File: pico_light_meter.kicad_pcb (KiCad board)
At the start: 2 copper layers, 52.5 x 27 mm, 5 parts

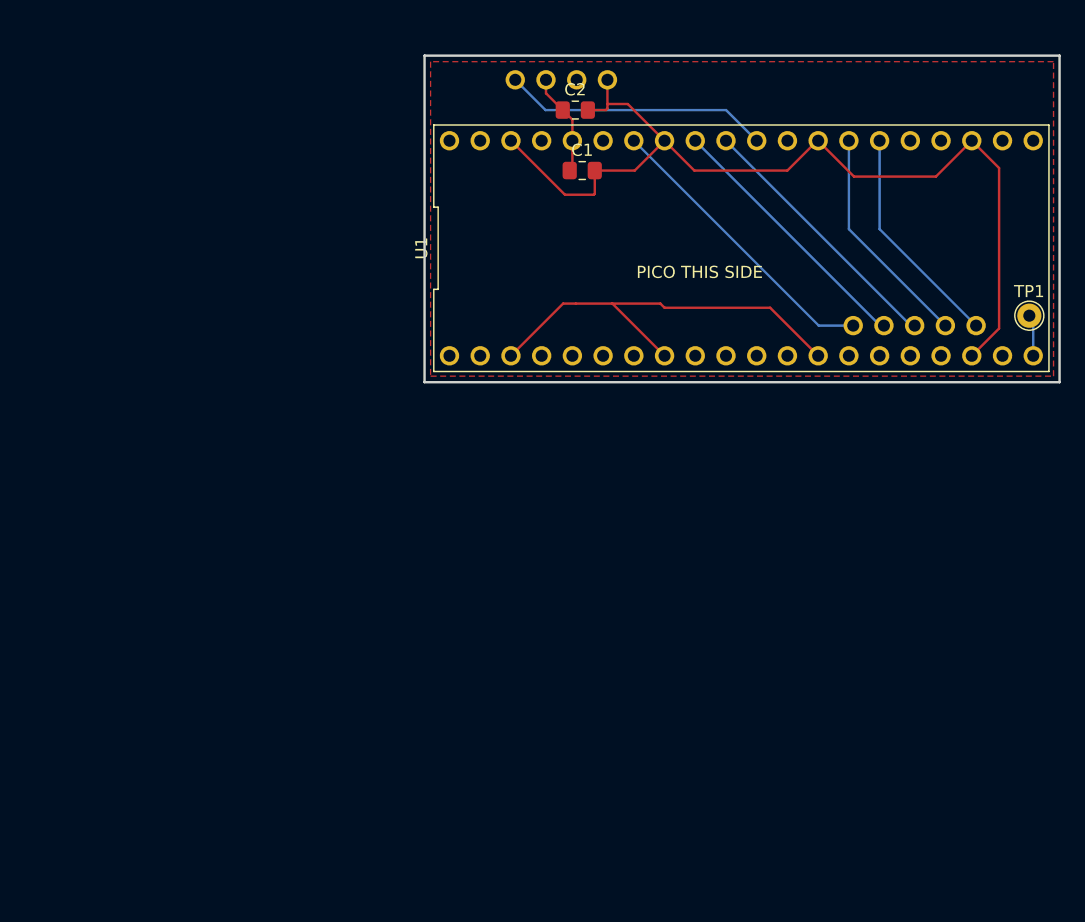
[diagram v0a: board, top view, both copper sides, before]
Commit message: Intermediate commit of routed board with Pico on top.
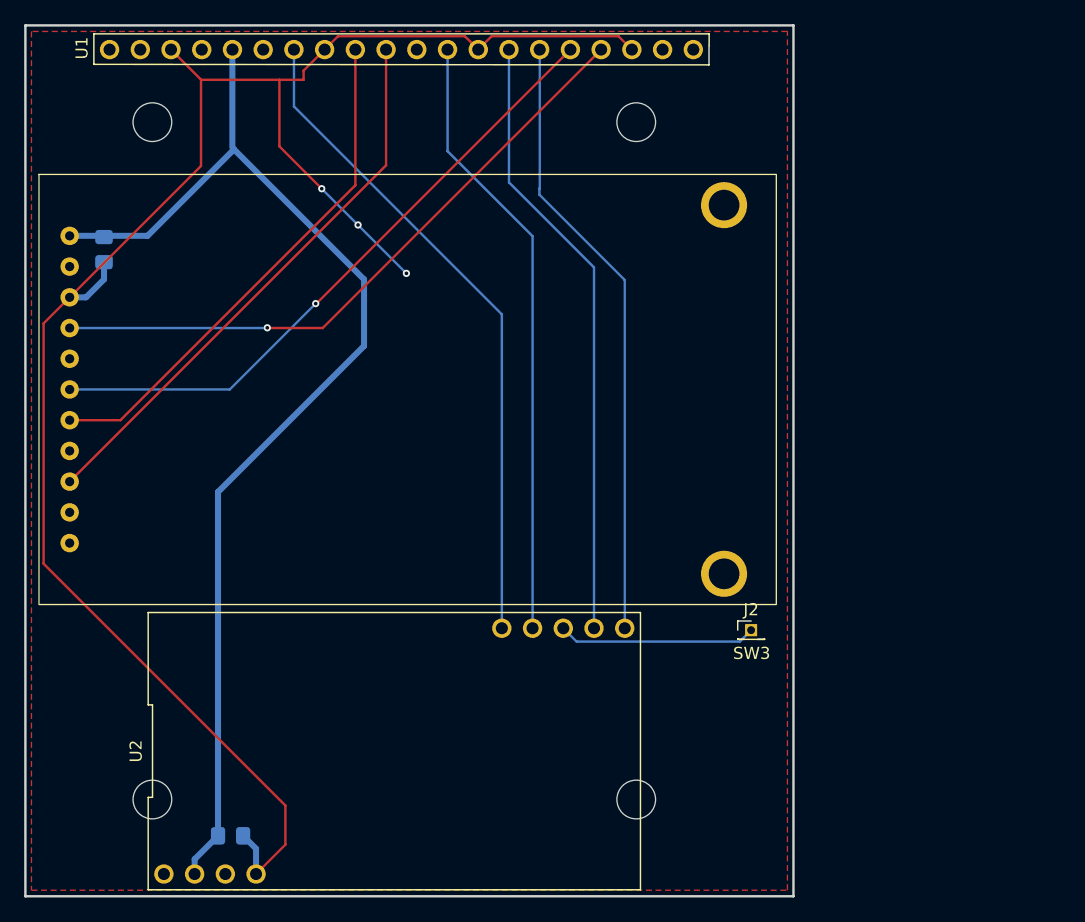
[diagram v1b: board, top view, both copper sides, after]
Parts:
- removed TP1: TestPoint, TestPoint:TestPoint_THTPad_D2.0mm_Drill1.0mm
- added H1: MountingHole, MountingHole:MountingHole_3.2mm_M3_ISO14580, F.Cu at (100.0, 50.0)
- added H2: MountingHole, MountingHole:MountingHole_3.2mm_M3_ISO14580, F.Cu at (140.0, 106.0)
- added H3: MountingHole, MountingHole:MountingHole_3.2mm_M3_ISO14580, F.Cu at (100.0, 106.0)
- added H4: MountingHole, MountingHole:MountingHole_3.2mm_M3_ISO14580, F.Cu at (140.0, 50.0)
- added J2: Conn_01x01, Connector_PinHeader_1.27mm:PinHeader_1x01_P1.27mm_Vertical, F.Cu at (149.5, 92.0)
- added U3: ~, pico_light_meter:adafruit_2.0_IPS_Display, F.Cu at (90.6, 54.3)
- C1, C2: moved to B.Cu
- U1: footprint pico_light_meter:pico2 -> pico_light_meter:pico2_right_pins_only
- U2: moved to F.Cu
- moved C2 66.4 mm to (106.5, 109.0)
- moved U2 53.8 mm to (120.0, 102.0)
- moved C1 40.1 mm to (96.0, 60.5), turned to -90 degrees
- moved U1 29.1 mm to (120.6, 52.9)
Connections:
- net /I2C0_SCL renamed /OLED_SCL
- net /I2C0_SDA renamed /OLED_SDA
- U1 pad 21: unconnected-(U1-_MISO-Pad21) -> /SD_MISO
- U1 pad 22: unconnected-(U1-_CARD_CS-Pad22) -> /SD_CS
- U1 pad 24: unconnected-(U1-_SCK-Pad24) -> /IPS_SCK
- U1 pad 25: unconnected-(U1-_MOSI-Pad25) -> /IPS_MOSI
- U1 pad 29: unconnected-(U1-_SHUTTER-Pad29) -> /COWBELL_SHUTTER
- U1 pad 31: /SW3 -> /IPS_DC
- U1 pad 32: /SW4 -> /IPS_CS
- U2 pad 1: //RESET -> unconnected-(U2-/RESET-Pad1)
- U2 pad 20: /SW4 -> /COWBELL_SHUTTER
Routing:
- net +3.3V: track 8.50 -> 95.0 mm
- net /IPS_SCK: track 0.00 -> 53.5 mm, vias 0 -> 1
- net /IPS_MOSI: track 0.00 -> 53.0 mm, vias 0 -> 1
- net /COWBELL_SHUTTER: track 0.00 -> 50.8 mm
- net /IPS_DC: track 0.00 -> 46.6 mm
- net /IPS_CS: track 0.00 -> 42.9 mm
- net GND: track 112.2 -> 151.6 mm, vias 0 -> 3
- net /OLED_SDA: track 18.6 -> 50.8 mm
- net /OLED_SCL: track 18.6 -> 50.8 mm
- net /SW2: track 24.5 -> 55.0 mm
- net //RESET: track 22.0 -> 0.00 mm
- net /SW4: track 21.9 -> 0.00 mm
- net /SW3: track 21.9 -> 16.4 mm
- net Net-(U1-GPIO15): track 3.45 -> 0.00 mm
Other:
- board size 52.5 x 27 mm -> 63.5 x 72 mm
- board text added: "SW3"
- board text removed: "OLED THIS SIDE"
- board text removed: "PICO THIS SIDE"

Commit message: Another iteration, now with Pico on bottom
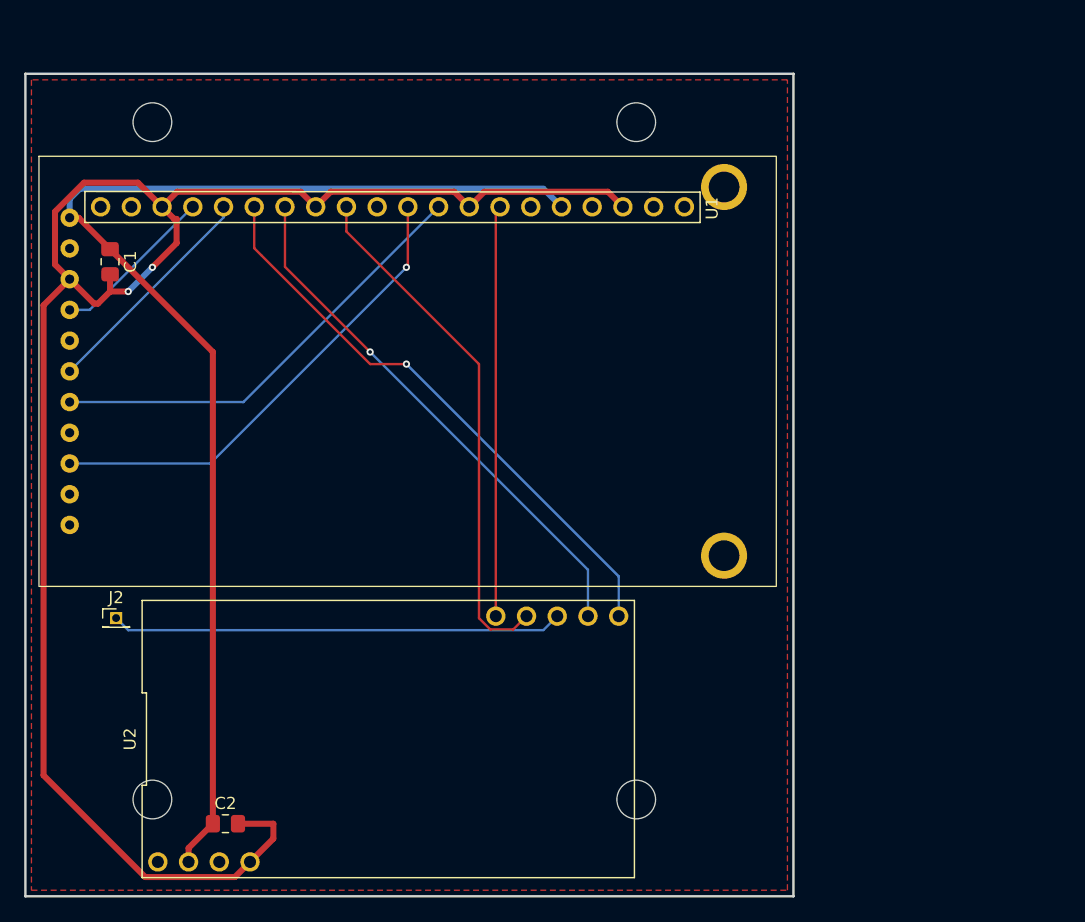
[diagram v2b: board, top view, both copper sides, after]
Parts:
- C1, C2: moved to F.Cu
- moved J2 52.5 mm to (97.0, 91.0)
- moved U1 4.84 mm to (119.8, 48.1), turned to 180 degrees
- moved U3 1.50 mm to (90.6, 52.8)
- moved C1 1.12 mm to (96.5, 61.5)
- moved U2 1.12 mm to (119.5, 101.0)
- moved C2 1.09 mm to (106.0, 108.0)
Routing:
- net /IPS_SCK: track 53.5 -> 13.7 mm, vias 1 -> 0
- net /IPS_MOSI: track 53.0 -> 18.9 mm, vias 1 -> 0
- net /SW3: track 16.4 -> 37.4 mm
- net /SW2: track 55.0 -> 34.0 mm
- net +3.3V: track 95.0 -> 102.6 mm
- net /COWBELL_SHUTTER: track 50.8 -> 43.3 mm
- net GND: track 151.6 -> 144.6 mm, vias 3 -> 2
- net /IPS_DC: track 46.6 -> 39.6 mm, vias 0 -> 1
- net /OLED_SCL: track 50.8 -> 44.2 mm, vias 0 -> 1
- net /IPS_CS: track 42.9 -> 37.2 mm
- net /OLED_SDA: track 50.8 -> 48.1 mm, vias 0 -> 1
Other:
- board size 63.5 x 72 mm -> 63.5 x 68 mm
- board text removed: "SW3"

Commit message: Updated with MCP port expander
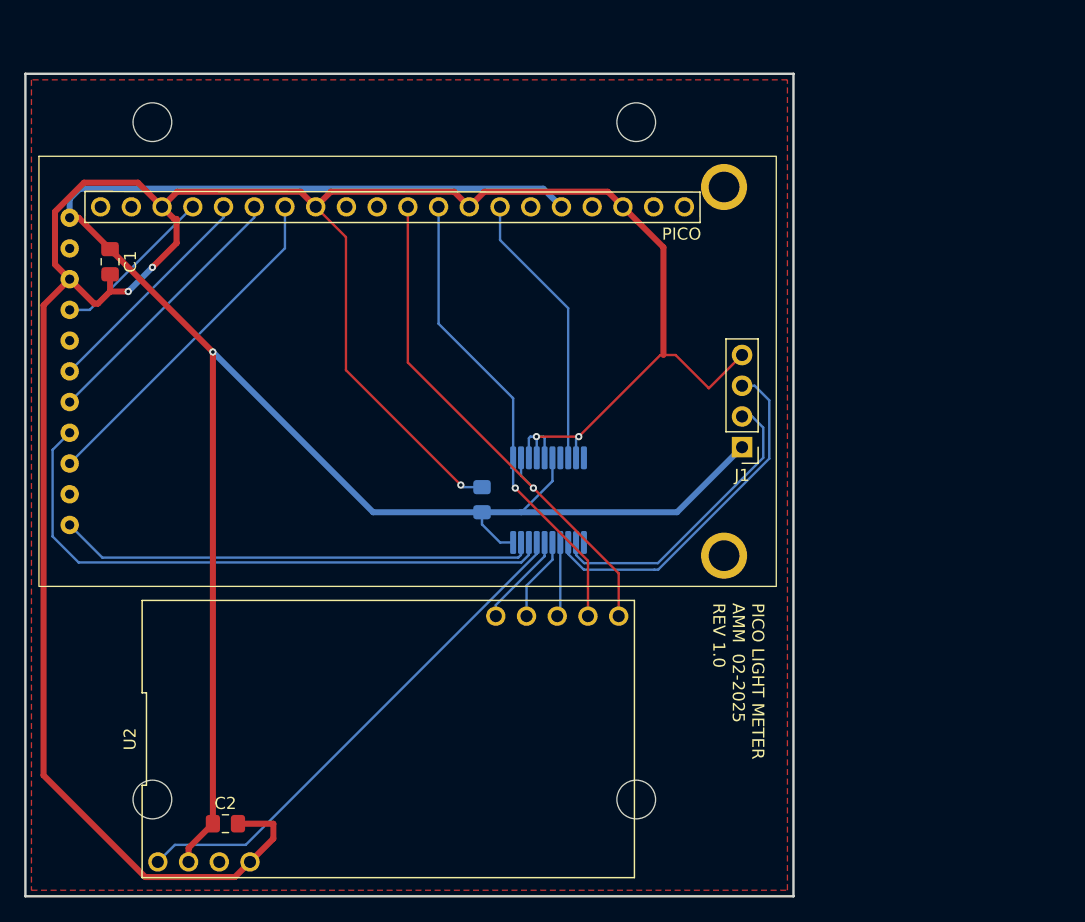
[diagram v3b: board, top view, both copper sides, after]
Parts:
- removed J2: Conn_01x01, Connector_PinHeader_1.27mm:PinHeader_1x01_P1.27mm_Vertical
- added C3: C, Capacitor_SMD:C_0805_2012Metric_Pad1.18x1.45mm_HandSolder, B.Cu at (127.2, 81.2)
- added J1: Conn_01x04, Connector_PinHeader_2.54mm:PinHeader_1x04_P2.54mm_Vertical, F.Cu at (148.8, 76.9)
- added U4: MCP23008-xSS, Package_SO:SSOP-20_5.3x7.2mm_P0.65mm, B.Cu at (132.8, 81.2)
- renumbered U1 to PICO
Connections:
- PICO pad 26: /OLED_SDA -> /IPS_CS
- PICO pad 27: /OLED_SCL -> /IPS_DC
- PICO pad 31: /IPS_DC -> /I2C1_SDA
- PICO pad 32: /IPS_CS -> /I2C1_SCL
- PICO pad 34: /SW2 -> /MCP_INT
- U2 pad 1: unconnected-(U2-/RESET-Pad1) -> /SW5
- U2 pad 17: /OLED_SDA -> /I2C1_SDA
- U2 pad 18: /OLED_SCL -> /I2C1_SCL
- U2 pad 20: /COWBELL_SHUTTER -> /SW4
- U3 pad 1: unconnected-(U3-BACKLIGHT-Pad1) -> /IPS_BACKLIGHT
- U3 pad 4: unconnected-(U3-RESET-Pad4) -> /IPS_RESET
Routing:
- net GND: track 144.6 -> 218.4 mm, vias 2 -> 5
- net +3.3V: track 102.6 -> 163.8 mm, vias 0 -> 1
- net /IPS_RESET: track 0.00 -> 50.7 mm
- net /OLED_SDA: track 48.1 -> 0.00 mm, vias 1 -> 0
- net /OLED_SCL: track 44.2 -> 0.00 mm, vias 1 -> 0
- net /I2C1_SDA: track 0.00 -> 44.0 mm, vias 0 -> 1
- net /COWBELL_SHUTTER: track 43.3 -> 0.00 mm
- net /SW5: track 0.00 -> 42.8 mm
- net /IPS_BACKLIGHT: track 0.00 -> 39.6 mm
- net /I2C1_SCL: track 0.00 -> 39.0 mm, vias 0 -> 1
- net /SW3: track 37.4 -> 6.20 mm
- net Net-(J1-Pin_3): track 0.00 -> 29.5 mm
- net /SW2: track 34.0 -> 7.92 mm
- net Net-(J1-Pin_2): track 0.00 -> 25.0 mm
- net /MCP_INT: track 0.00 -> 23.6 mm
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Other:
- board text added: "PICO LIGHT METER AMM 02-2025 REV 1.0"

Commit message: Big update to board
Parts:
- C1, C2: moved to B.Cu
- C3, U4: moved to F.Cu
- U3: footprint pico_light_meter:adafruit_2.0_IPS_Display -> pico_light_meter:adafruit_2.0_IPS_Display_minimal
- moved U3 49.6 mm to (138.2, 66.7), turned to -90 degrees
- moved U2 46.5 mm to (120.0, 54.5)
- moved C2 42.8 mm to (130.4, 72.8), turned to 180 degrees
- moved C3 36.0 mm to (125.0, 45.2), turned to 180 degrees
- moved U4 31.9 mm to (125.2, 50.3), turned to 0 degrees
- moved C1 9.56 mm to (106.0, 62.2), turned to 0 degrees
- moved J1 7.83 mm to (143.2, 71.3)
- renumbered PICO to U1
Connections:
- U1 pad 26: /IPS_CS -> /IPS_DC
- U1 pad 27: /IPS_DC -> /IPS_CS
- U4 pad 12: Net-(J1-Pin_2) -> Net-(J1-Pin_3)
- U4 pad 13: Net-(J1-Pin_3) -> Net-(J1-Pin_2)
- U4 pad 14: /SW3 -> /IPS_RESET
- U4 pad 15: /SW4 -> /IPS_BACKLIGHT
- U4 pad 16: /SW2 -> /SW3
- U4 pad 17: /SW5 -> /SW4
- U4 pad 18: /IPS_RESET -> /SW2
- U4 pad 19: /IPS_BACKLIGHT -> /SW5
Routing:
- net GND: track 218.4 -> 127.1 mm, vias 5 -> 0
- net +3.3V: track 163.8 -> 90.9 mm, vias 1 -> 4
- net /IPS_SCK: track 13.7 -> 34.5 mm
- net /IPS_RESET: track 50.7 -> 33.0 mm, vias 0 -> 1
- net /I2C1_SDA: track 44.0 -> 28.8 mm
- net /IPS_DC: track 28.6 -> 14.1 mm
- net /I2C1_SCL: track 39.0 -> 25.7 mm, vias 1 -> 0
- net Net-(J1-Pin_2): track 25.0 -> 32.8 mm
- net /IPS_MOSI: track 18.9 -> 26.5 mm
- net /IPS_CS: track 22.5 -> 15.1 mm
- net /MCP_INT: track 23.6 -> 19.8 mm
- net /SW3: track 6.20 -> 9.21 mm, vias 0 -> 1
- net /SW5: track 42.8 -> 40.7 mm, vias 0 -> 1
- net /IPS_BACKLIGHT: track 39.6 -> 38.0 mm, vias 0 -> 1
- net /SW2: track 7.92 -> 6.58 mm, vias 0 -> 1
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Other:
- board size 63.5 x 68 mm -> 53.8 x 68.2 mm
